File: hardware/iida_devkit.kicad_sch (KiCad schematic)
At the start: 7 parts

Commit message: HW: Refine schema
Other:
- note added: "Place a fiducial marker at the top-right, bottom-right and bottom-left corners."
- note added: "There's no real chassis or a case to mount the PCB, so just place the mounting holes at the corners of the PCB."
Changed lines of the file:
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@@
+		)
+	)
+	(text "There's no real chassis or a case to mount the PCB,\nso just place the mounting holes at the corners of the PCB."
+		(exclude_from_sim no)
+		(at 108.458 179.07 0)
+		(effects
+			(font
+				(size 1.27 1.27)
+			)
+			(justify left)
+		)
+	)
+	(text "Place a fiducial marker at the top-right,\nbottom-right and bottom-left corners."
+		(exclude_from_sim no)
+		(at 114.046 167.132 0)
+		(effects
+			(font
+				(size 1.27 1.27)
+			)
+			(justify left)
 		)
 	)
@@
 		(dnp no)
 		(property "Reference" "FID2"
-			(at 132.715 170.18 0)
+			(at 132.334 170.18 0)
 			(effects
 				(font
@@
 			)
 		)
-		(pin "ANT" input
+		(pin "ANT" bidirectional
 			(at 120.65 114.3 180)
 			(effects
@@
 			)
 		)
-		(pin "ANT" output
+		(pin "ANT" bidirectional
 			(at 114.3 114.3 0)
 			(effects

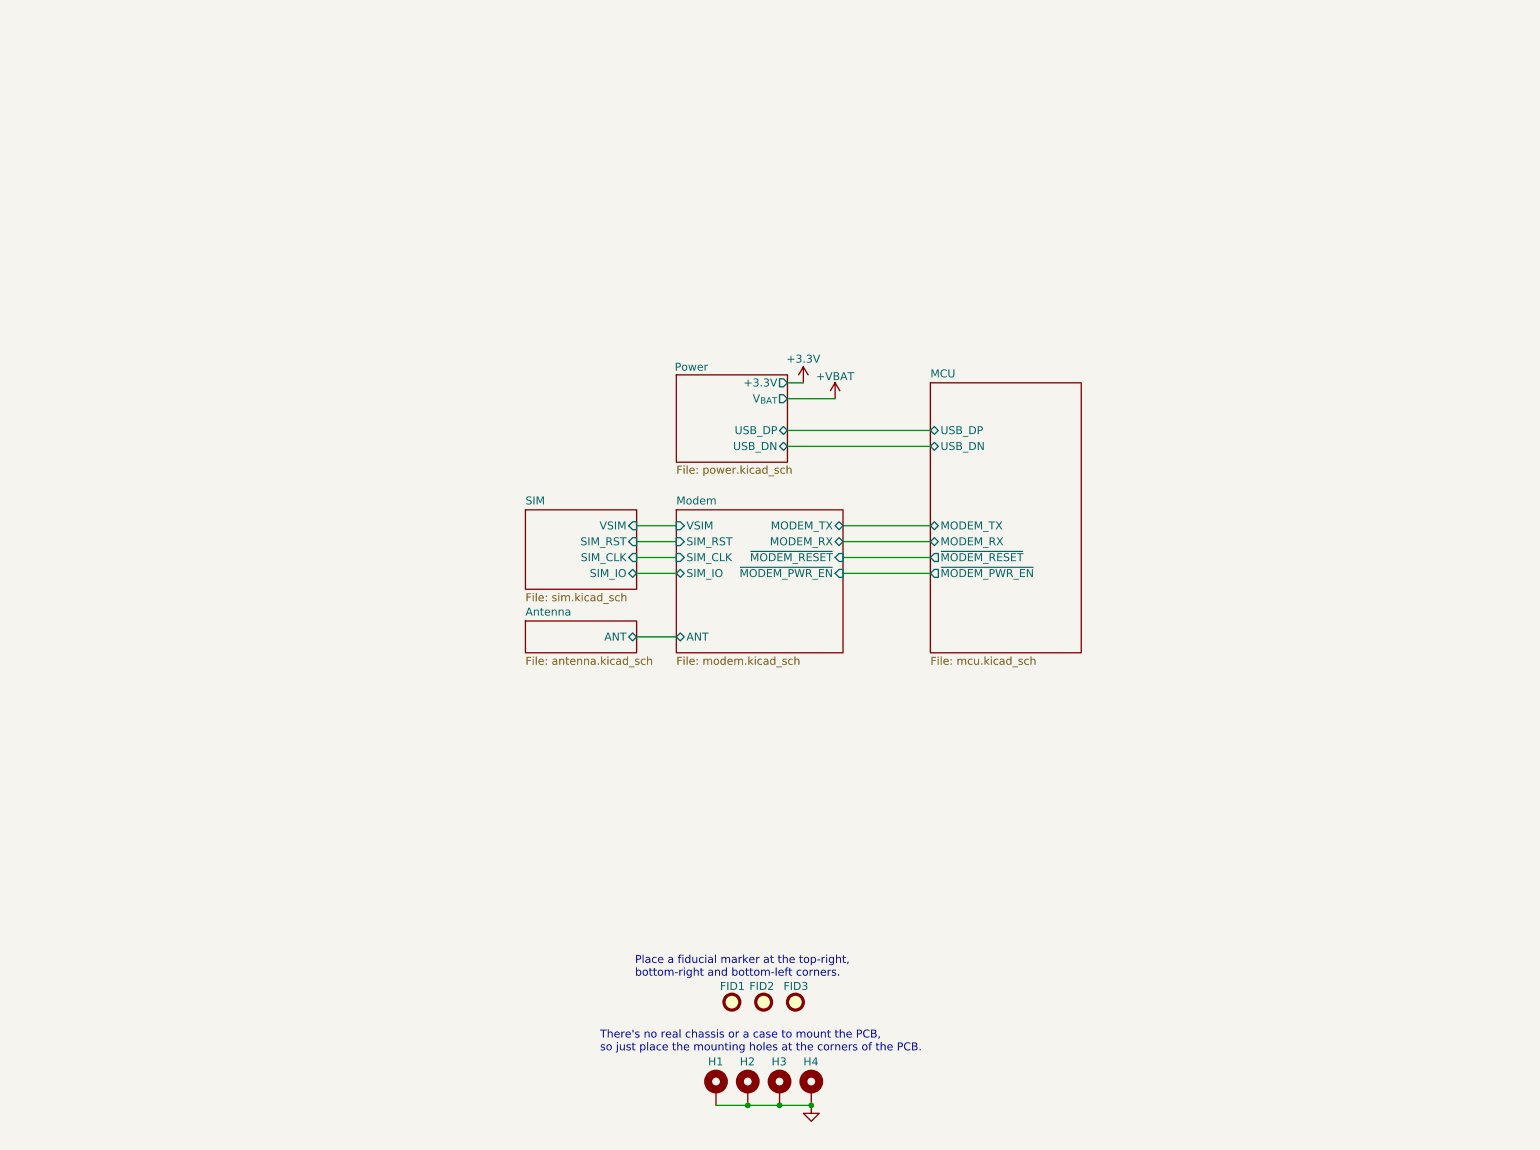
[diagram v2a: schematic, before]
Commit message: HW: Add project description to main schema sheet
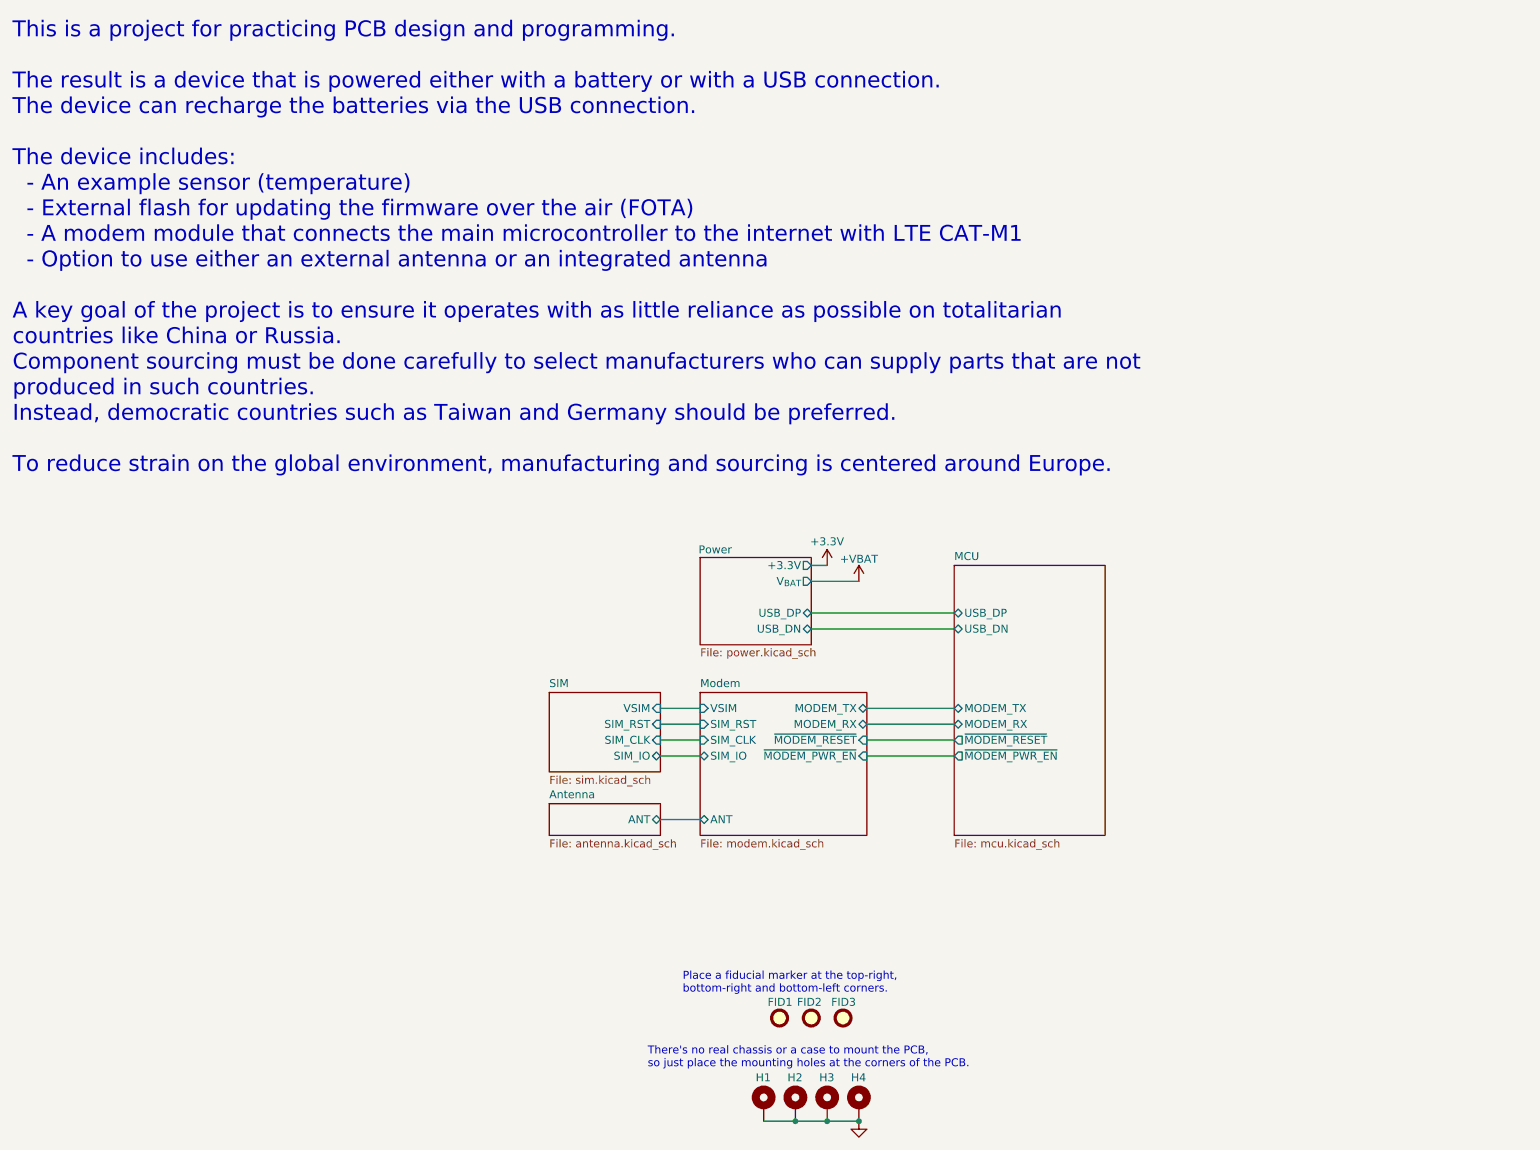
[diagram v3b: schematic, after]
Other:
- note added: "This is a project for practicing PCB design and programming. The result is a device that is powered either with a battery or with a USB connection. The device can recharge the batteries via the USB connection. The device includes: - An example sensor (temperature) - External flash for updating the firmware over the air (FOTA) - A modem module that connects the main microcontroller to the internet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"
- moved on the sheet: FID1, FID2, FID3, H1, H2, H3, H4
